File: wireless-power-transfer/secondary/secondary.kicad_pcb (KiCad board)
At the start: 2 copper layers, 100 x 60 mm, 10 parts, among them J1 Screw_Terminal_1x02, J2 Screw_Terminal_1x02, U1 LM7812CT

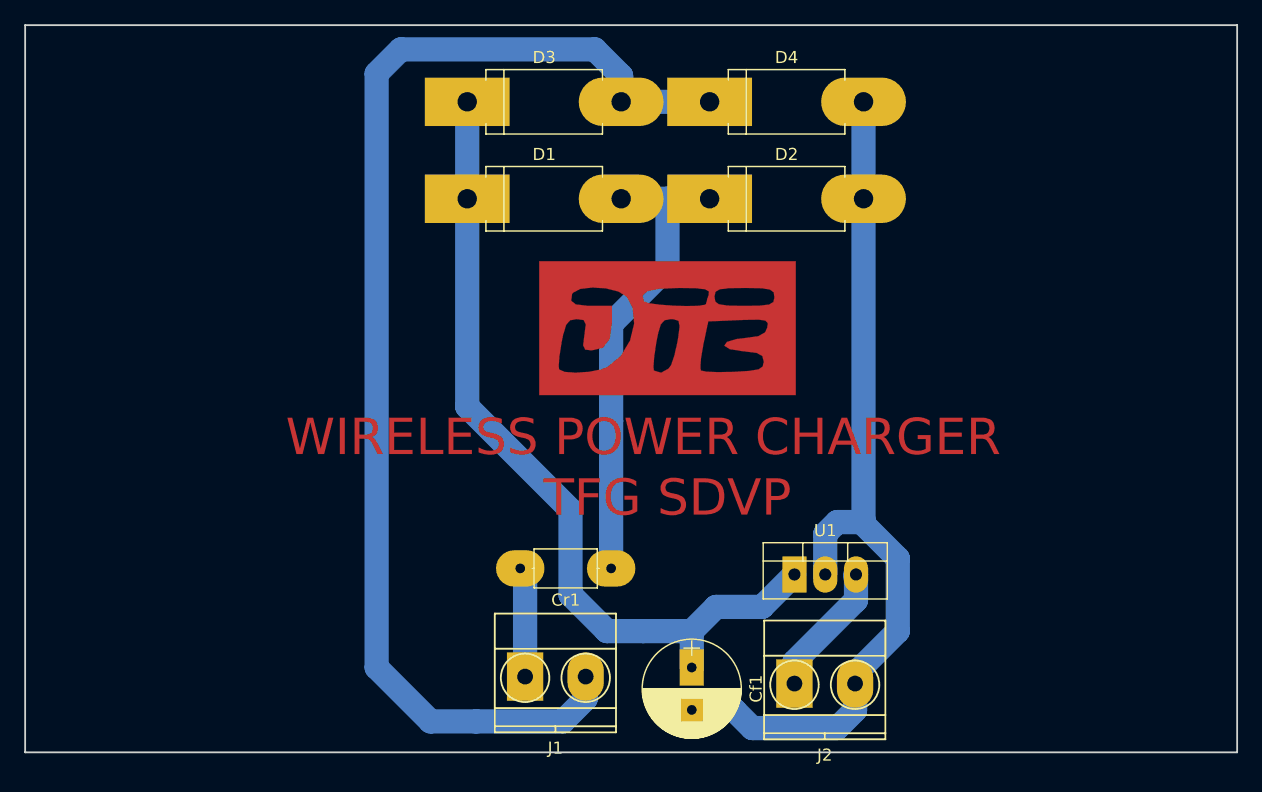
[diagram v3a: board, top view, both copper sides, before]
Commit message: PCB size modified. Added marks for mounting holes.
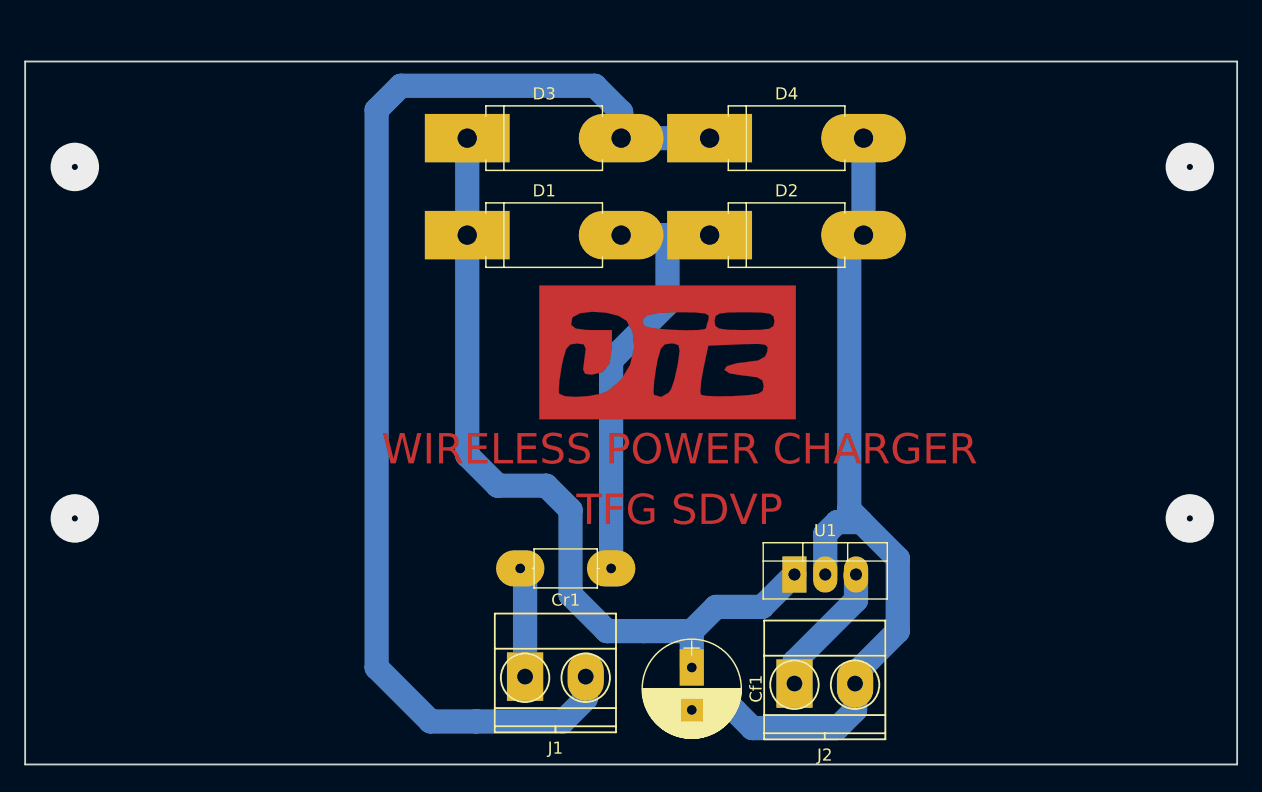
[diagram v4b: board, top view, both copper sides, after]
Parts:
- moved D1 3.00 mm to (120.5, 71.3)
- moved D2 3.00 mm to (140.5, 71.3)
- moved D3 3.00 mm to (120.5, 63.3)
- moved D4 3.00 mm to (140.5, 63.3)
- moved G*** 2.00 mm to (137.0, 81.0)
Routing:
- net Net-(Cr1-Pad1): track 39.7 -> 36.7 mm
- net Net-(D3-Pad2): track 102.0 -> 99.0 mm
- net Net-(Cf1-Pad2): track 74.8 -> 74.0 mm
- net Net-(Cf1-Pad1): track 68.9 -> 68.2 mm
- net (no net): vias 0 -> 4
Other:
- board size 100 x 60 mm -> 100 x 58 mm
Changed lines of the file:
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@@
     (thickness 1.6)
     (drawings 6)
-    (tracks 51)
+    (tracks 57)
     (zones 0)
     (modules 10)
@@
   )
   (setup
-    (last_trace_width 0.25)
+    (last_trace_width 2)
     (user_trace_width 0.8)
     (user_trace_width 2)
@@
     (via_min_size 0.4)
     (via_min_drill 0.3)
+    (user_via 4 0.5)
     (uvia_size 0.3)
     (uvia_drill 0.1)
@@
   )
   (module Diodes_THT:D_DO-201AD_P12.70mm_Horizontal (layer F.Cu)
-    (at 120.475 68.325)
+    (at 120.475 71.325)
     (descr "D, DO-201AD series, Axial, Horizontal, pin pitch=12.7mm, , length*diameter=9.5*5.2mm^2, , http://www.diodes.com/_files/packages/DO-201AD.pdf")
     (tags "D DO-201AD series Axial Horizontal pin pitch 12.7mm  length 9.5mm diameter 5.2mm")
@@
   )
   (module Diodes_THT:D_DO-201AD_P12.70mm_Horizontal (layer F.Cu)
-    (at 140.475 68.325)
+    (at 140.475 71.325)
     (descr "D, DO-201AD series, Axial, Horizontal, pin pitch=12.7mm, , length*diameter=9.5*5.2mm^2, , http://www.diodes.com/_files/packages/DO-201AD.pdf")
     (tags "D DO-201AD series Axial Horizontal pin pitch 12.7mm  length 9.5mm diameter 5.2mm")
@@
   )
   (module Diodes_THT:D_DO-201AD_P12.70mm_Horizontal (layer F.Cu)
-    (at 120.475 60.325)
+    (at 120.475 63.325)
     (descr "D, DO-201AD series, Axial, Horizontal, pin pitch=12.7mm, , length*diameter=9.5*5.2mm^2, , http://www.diodes.com/_files/packages/DO-201AD.pdf")
     (tags "D DO-201AD series Axial Horizontal pin pitch 12.7mm  length 9.5mm diameter 5.2mm")
@@
   )
   (module Diodes_THT:D_DO-201AD_P12.70mm_Horizontal (layer F.Cu)
-    (at 140.475 60.325)
+    (at 140.475 63.325)
     (descr "D, DO-201AD series, Axial, Horizontal, pin pitch=12.7mm, , length*diameter=9.5*5.2mm^2, , http://www.diodes.com/_files/packages/DO-201AD.pdf")
     (tags "D DO-201AD series Axial Horizontal pin pitch 12.7mm  length 9.5mm diameter 5.2mm")
@@
   )
   (module componentes:DTE (layer F.Cu)
-    (at 137 79)
+    (at 137 81)
     (fp_text reference G*** (at 14 1) (layer F.SilkS) hide
       (effects (font (thickness 0.3)))
@@
       (xy 10.583333 5.521739)) (layer F.Cu) (width 0.01))
   )
-  (gr_text "TFG SDVP" (at 137 93) (layer F.Cu)
-    (effects (font (size 3 3) (thickness 0.5)))
-  )
-  (gr_text "WIRELESS POWER CHARGER" (at 135 88) (layer F.Cu)
-    (effects (font (size 3 3) (thickness 0.5)))
-  )
-  (gr_line (start 84 114) (end 84 54) (angle 90) (layer Edge.Cuts) (width 0.15))
-  (gr_line (start 184 114) (end 84 114) (angle 90) (layer Edge.Cuts) (width 0.15))
-  (gr_line (start 184 54) (end 184 114) (angle 90) (layer Edge.Cuts) (width 0.15))
-  (gr_line (start 84 54) (end 184 54) (angle 90) (layer Edge.Cuts) (width 0.15))
-  (segment (start 120.475 68.325) (end 120.475 85.475) (width 2) (layer B.Cu) (net 1))
-  (segment (start 129 94) (end 120.475 85.475) (width 2) (layer B.Cu) (net 1))
+  (gr_line (start 84 115) (end 84 57) (angle 90) (layer Edge.Cuts) (width 0.15))
+  (gr_line (start 184 115) (end 84 115) (angle 90) (layer Edge.Cuts) (width 0.15))
+  (gr_line (start 184 57) (end 184 115) (angle 90) (layer Edge.Cuts) (width 0.15))
+  (gr_line (start 84 57) (end 184 57) (angle 90) (layer Edge.Cuts) (width 0.15))
+  (gr_text "TFG SDVP" (at 138 94) (layer F.Cu)
+    (effects (font (size 2.5 2.5) (thickness 0.5)))
+  )
+  (gr_text "WIRELESS POWER CHARGER" (at 138 89) (layer F.Cu)
+    (effects (font (size 2.5 2.5) (thickness 0.5)))
+  )
+  (via (at 88.1 65.7) (size 4) (drill 0.5) (layers F.Cu B.Cu) (net 0))
+  (via (at 88.1 94.7) (size 4) (drill 0.5) (layers F.Cu B.Cu) (net 0))
+  (via (at 180.1 94.7) (size 4) (drill 0.5) (layers F.Cu B.Cu) (net 0))
+  (via (at 180.1 65.7) (size 4) (drill 0.5) (layers F.Cu B.Cu) (net 0))
+  (segment (start 129 94) (end 127 92) (width 2) (layer B.Cu) (net 1))
+  (segment (start 139 104) (end 135 104) (width 2) (layer B.Cu) (net 1))
+  (segment (start 135 104) (end 132 104) (width 2) (layer B.Cu) (net 1))
+  (segment (start 132 104) (end 129 101) (width 2) (layer B.Cu) (net 1))
   (segment (start 129 101) (end 129 94) (width 2) (layer B.Cu) (net 1))
-  (segment (start 132 104) (end 129 101) (width 2) (layer B.Cu) (net 1))
-  (segment (start 135 104) (end 132 104) (width 2) (layer B.Cu) (net 1))
-  (segment (start 135 104) (end 139 104) (width 2) (layer B.Cu) (net 1))
-  (segment (start 120.475 68.325) (end 120.475 60.325) (width 2) (layer B.Cu) (net 1))
+  (segment (start 120.475 89.475) (end 120.475 71.325) (width 2) (layer B.Cu) (net 1))
+  (segment (start 123 92) (end 120.475 89.475) (width 2) (layer B.Cu) (net 1))
+  (segment (start 127 92) (end 123 92) (width 2) (layer B.Cu) (net 1))
+  (segment (start 120.475 71.325) (end 120.475 63.325) (width 2) (layer B.Cu) (net 1))
   (segment (start 139 107) (end 139 104) (width 2) (layer B.Cu) (net 1))
   (segment (start 144.8 102) (end 147.475 99.325) (width 2) (layer B.Cu) (net 1))
   (segment (start 139 104) (end 141 102) (width 2) (layer B.Cu) (net 1))
   (segment (start 141 102) (end 144.8 102) (width 2) (layer B.Cu) (net 1))
-  (segment (start 153.175 68.325) (end 153.175 94.825) (width 2) (layer B.Cu) (net 2))
-  (segment (start 153.175 94.825) (end 153 95) (width 2) (layer B.Cu) (net 2))
-  (segment (start 153.175 68.325) (end 153.175 60.325) (width 2) (layer B.Cu) (net 2))
-  (segment (start 153 68.5) (end 153.175 68.325) (width 2) (layer B.Cu) (net 2))
+  (segment (start 152 94) (end 152 72.5) (width 2) (layer B.Cu) (net 2))
+  (segment (start 152 72.5) (end 153.175 71.325) (width 2) (layer B.Cu) (net 2))
+  (segment (start 153.175 71.325) (end 153.175 63.325) (width 2) (layer B.Cu) (net 2))
+  (segment (start 153 71.5) (end 153.175 71.325) (width 2) (layer B.Cu) (net 2))
   (segment (start 152.475 108.325) (end 152.475 107.525) (width 2) (layer B.Cu) (net 2))
   (segment (start 152.475 107.525) (end 156 104) (width 2) (layer B.Cu) (net 2))
   (segment (start 156 104) (end 156 98) (width 2) (layer B.Cu) (net 2))
-  (segment (start 156 98) (end 153 95) (width 2) (layer B.Cu) (net 2))
+  (segment (start 156 98) (end 152 94) (width 2) (layer B.Cu) (net 2))
+  (segment (start 152 94) (end 153 95) (width 2) (layer B.Cu) (net 2))
   (segment (start 150.015 95.985) (end 150.015 99.325) (width 2) (layer B.Cu) (net 2))
   (segment (start 153 95) (end 151 95) (width 2) (layer B.Cu) (net 2))
@@
   (segment (start 142.5 110.5) (end 144 112) (width 2) (layer B.Cu) (net 2))
   (segment (start 152.555 108.245) (end 152.475 108.325) (width 2) (layer B.Cu) (net 2))
-  (segment (start 132.35 86.65) (end 132.35 78.65) (width 2) (layer B.Cu) (net 3))
-  (segment (start 132.35 98.825) (end 132.35 86.65) (width 2) (layer B.Cu) (net 3))
-  (segment (start 137 74) (end 137 68.325) (width 2) (layer B.Cu) (net 3))
-  (segment (start 132.35 78.65) (end 137 74) (width 2) (layer B.Cu) (net 3))
-  (segment (start 140.475 68.325) (end 137 68.325) (width 2) (layer B.Cu) (net 3))
-  (segment (start 137 68.325) (end 133.175 68.325) (width 2) (layer B.Cu) (net 3))
+  (segment (start 132.35 98.825) (end 132.35 81.65) (width 2) (layer B.Cu) (net 3))
+  (segment (start 132.35 81.65) (end 137 77) (width 2) (layer B.Cu) (net 3))
+  (segment (start 137 77) (end 137 71.325) (width 2) (layer B.Cu) (net 3))
+  (segment (start 140.475 71.325) (end 137 71.325) (width 2) (layer B.Cu) (net 3))
+  (segment (start 137 71.325) (end 133.175 71.325) (width 2) (layer B.Cu) (net 3))
   (segment (start 125.25 107.75) (end 125.25 99.225) (width 2) (layer B.Cu) (net 4))
   (segment (start 125.25 99.225) (end 124.85 98.825) (width 2) (layer B.Cu) (net 4))
-  (segment (start 131 56) (end 115 56) (width 2) (layer B.Cu) (net 5))
-  (segment (start 130.25 109.575) (end 128.375 111.45) (width 2) (layer B.Cu) (net 5))
+  (segment (start 113 61) (end 113 107) (width 2) (layer B.Cu) (net 5))
+  (segment (start 115 59) (end 113 61) (width 2) (layer B.Cu) (net 5))
+  (segment (start 113 107) (end 117.45 111.45) (width 2) (layer B.Cu) (net 5))
+  (segment (start 117.45 111.45) (end 121.225 111.45) (width 2) (layer B.Cu) (net 5))
+  (segment (start 133.175 63.325) (end 133.175 61.175) (width 2) (layer B.Cu) (net 5))
+  (segment (start 131 59) (end 133.175 61.175) (width 2) (layer B.Cu) (net 5))
   (segment (start 128.375 111.45) (end 121.225 111.45) (width 2) (layer B.Cu) (net 5))
+  (segment (start 128.375 111.45) (end 130.25 109.575) (width 2) (layer B.Cu) (net 5))
+  (segment (start 131 59) (end 115 59) (width 2) (layer B.Cu) (net 5))
   (segment (start 130.25 107.75) (end 130.25 109.575) (width 2) (layer B.Cu) (net 5))
-  (segment (start 131 56) (end 133.175 58.175) (width 2) (layer B.Cu) (net 5))
-  (segment (start 133.175 58.175) (end 133.175 60.325) (width 2) (layer B.Cu) (net 5))
-  (segment (start 117.45 111.45) (end 121.225 111.45) (width 2) (layer B.Cu) (net 5))
-  (segment (start 113 107) (end 117.45 111.45) (width 2) (layer B.Cu) (net 5))
-  (segment (start 113 58) (end 113 107) (width 2) (layer B.Cu) (net 5))
-  (segment (start 115 56) (end 113 58) (width 2) (layer B.Cu) (net 5))
-  (segment (start 133.175 60.325) (end 140.475 60.325) (width 2) (layer B.Cu) (net 5))
+  (segment (start 133.175 63.325) (end 140.475 63.325) (width 2) (layer B.Cu) (net 5))
   (segment (start 147.475 108.325) (end 147.475 106.525) (width 2) (layer B.Cu) (net 6))
   (segment (start 152.555 101.445) (end 152.555 99.325) (width 2) (layer B.Cu) (net 6))

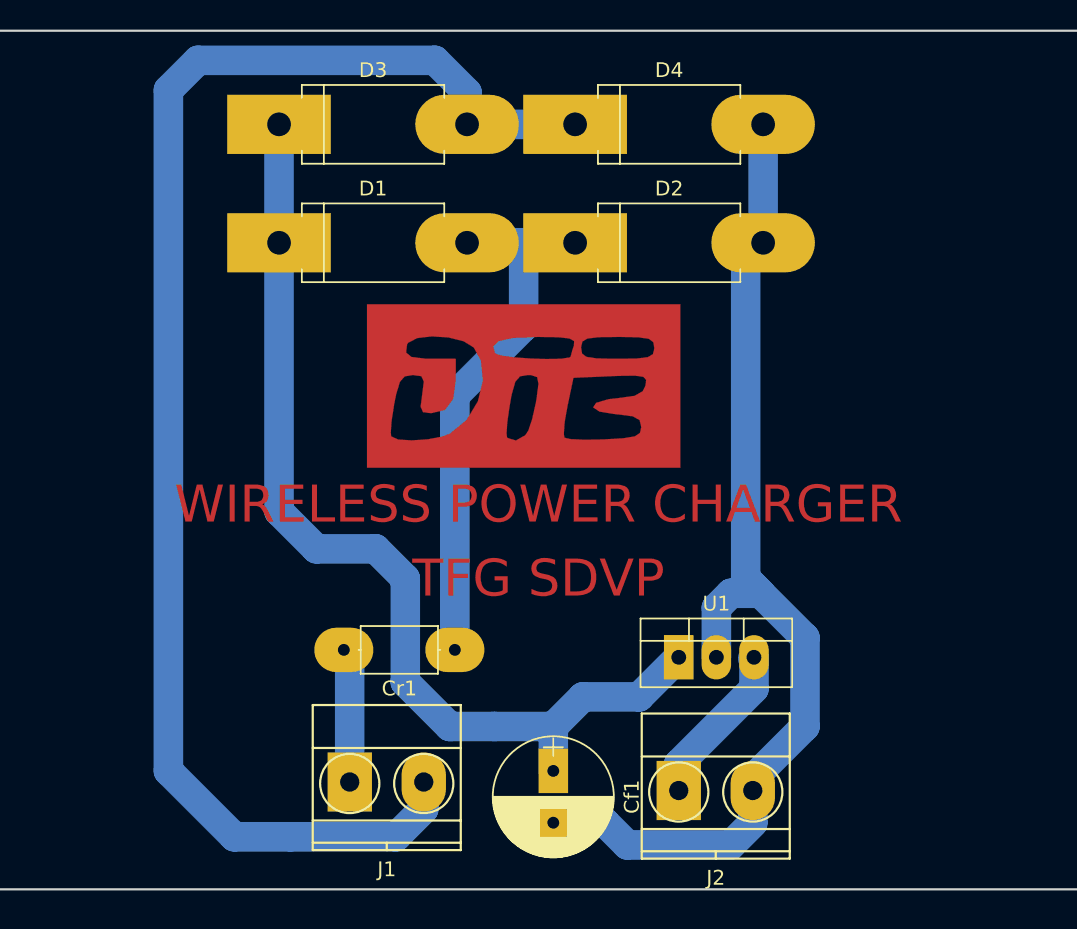
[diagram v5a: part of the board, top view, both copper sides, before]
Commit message: Prepare Silk Layer in order to be able to manufacture
This 'manu2' branch was created in order to have the 3 projects
on the same folder.

The silk layer was created and adapted to give it to an external
manufacturer.
Nearly the same information was created in the copper layer in order to
have this information also in the case the PCB's were manufactured in
the DTE.
The Mask layer was also adapted to give it to the external manufacturer.
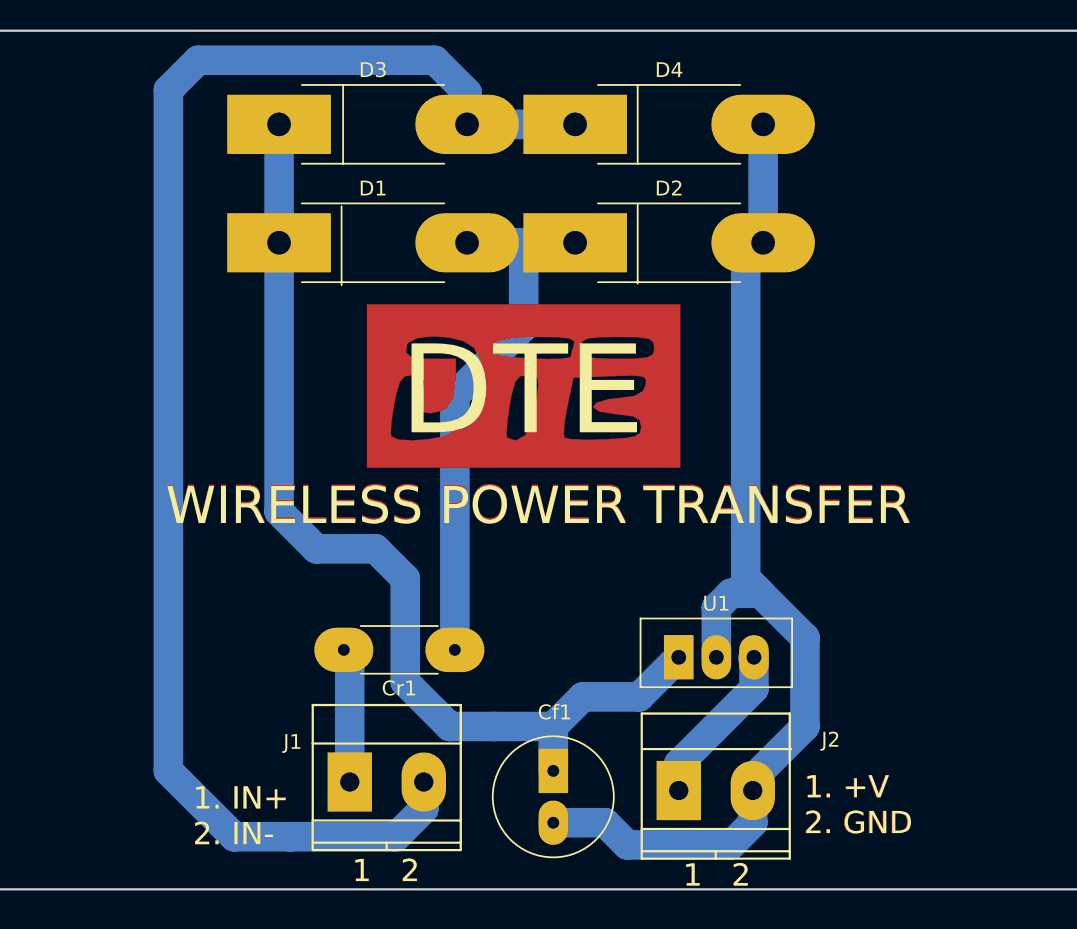
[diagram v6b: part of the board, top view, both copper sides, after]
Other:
- rule pad_to_mask_clearance: 0.2 -> 0.1
- board text added: "1 2"
- board text added: "1. +V 2. GND"
- board text added: "1. IN+ 2. IN-"
- board text added: "DTE"
- board text added: "WIRELESS POWER TRANSFER"
- board text removed: "TFG SDVP"
- board text removed: "WIRELESS POWER CHARGER"
